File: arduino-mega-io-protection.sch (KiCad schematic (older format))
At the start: 29 parts, among them J101 CONN_01X02, J102 CONN_01X02, J103 CONN_01X02, J104 CONN_01X02, J105 CONN_01X02, J106 CONN_01X02, J107 CONN_01X02, J108 CONN_01X36, J109 CONN_01X10, J110 CONN_02X18, J111 CONN_01X08, J112 CONN_01X08, J113 CONN_01X08, J114 CONN_01X08, J115 CONN_01X08

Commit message: inserting part information for connectors into BOM
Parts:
- J109: MFN Value -> Sullins Connector Solutions; MPN Value -> PRPC010SAAN-RC; Populate (none) -> 1
- J112: MFN Value -> Sullins Connector Solutions; MPN Value -> PRPC008SAAN-RC; Populate (none) -> 1
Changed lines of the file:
@@
 F 2 "Pin_Headers:Pin_Header_Straight_1x10_Pitch2.54mm" H 9850 2250 50  0001 C CNN
 F 3 "" H 9850 2250 50  0001 C CNN
-F 4 "Value" H 9850 2250 60  0001 C CNN "MPN"
-F 5 "Value" H 9850 2250 60  0001 C CNN "MFN"
-F 6 "Value" H 9850 2250 60  0001 C CNN "Characteristics"
-F 7 "Value" H 9850 2250 60  0001 C CNN "Description"
-F 8 "Value" H 9850 2250 60  0001 C CNN "Package ID"
-F 9 "Digikey" H 9850 2250 60  0001 C CNN "Source"
-F 10 "Y" H 9850 2250 60  0001 C CNN "Critical"
-F 11 "X" H 9850 2250 60  0001 C CNN "Notes"
+F 4 "Value" H 9850 2250 60  0001 C CNN "Characteristics"
+F 5 "Value" H 9850 2250 60  0001 C CNN "Description"
+F 6 "Sullins Connector Solutions" H 9850 2250 60  0001 C CNN "MFN"
+F 7 "Value" H 9850 2250 60  0001 C CNN "Package ID"
+F 8 "Digikey" H 9850 2250 60  0001 C CNN "Source"
+F 9 "Y" H 9850 2250 60  0001 C CNN "Critical"
+F 10 "X" H 9850 2250 60  0001 C CNN "Notes"
+F 11 "1" H 9850 2250 60  0001 C CNN "Populate"
+F 12 "PRPC010SAAN-RC" H 9850 2250 60  0001 C CNN "MPN"
 	1    9850 2250
 	1    0    0    -1
@@
 F 2 "Pin_Headers:Pin_Header_Straight_1x08_Pitch2.54mm" H 9850 3250 50  0001 C CNN
 F 3 "" H 9850 3250 50  0001 C CNN
-F 4 "Value" H 9850 3250 60  0001 C CNN "MPN"
-F 5 "Value" H 9850 3250 60  0001 C CNN "MFN"
-F 6 "Value" H 9850 3250 60  0001 C CNN "Characteristics"
-F 7 "Value" H 9850 3250 60  0001 C CNN "Description"
-F 8 "Value" H 9850 3250 60  0001 C CNN "Package ID"
-F 9 "Digikey" H 9850 3250 60  0001 C CNN "Source"
-F 10 "Y" H 9850 3250 60  0001 C CNN "Critical"
-F 11 "X" H 9850 3250 60  0001 C CNN "Notes"
+F 4 "Value" H 9850 3250 60  0001 C CNN "Characteristics"
+F 5 "Value" H 9850 3250 60  0001 C CNN "Description"
+F 6 "Sullins Connector Solutions" H 9850 3250 60  0001 C CNN "MFN"
+F 7 "Value" H 9850 3250 60  0001 C CNN "Package ID"
+F 8 "Digikey" H 9850 3250 60  0001 C CNN "Source"
+F 9 "Y" H 9850 3250 60  0001 C CNN "Critical"
+F 10 "X" H 9850 3250 60  0001 C CNN "Notes"
+F 11 "1" H 9850 3250 60  0001 C CNN "Populate"
+F 12 "PRPC008SAAN-RC" H 9850 3250 60  0001 C CNN "MPN"
 	1    9850 3250
 	1    0    0    -1

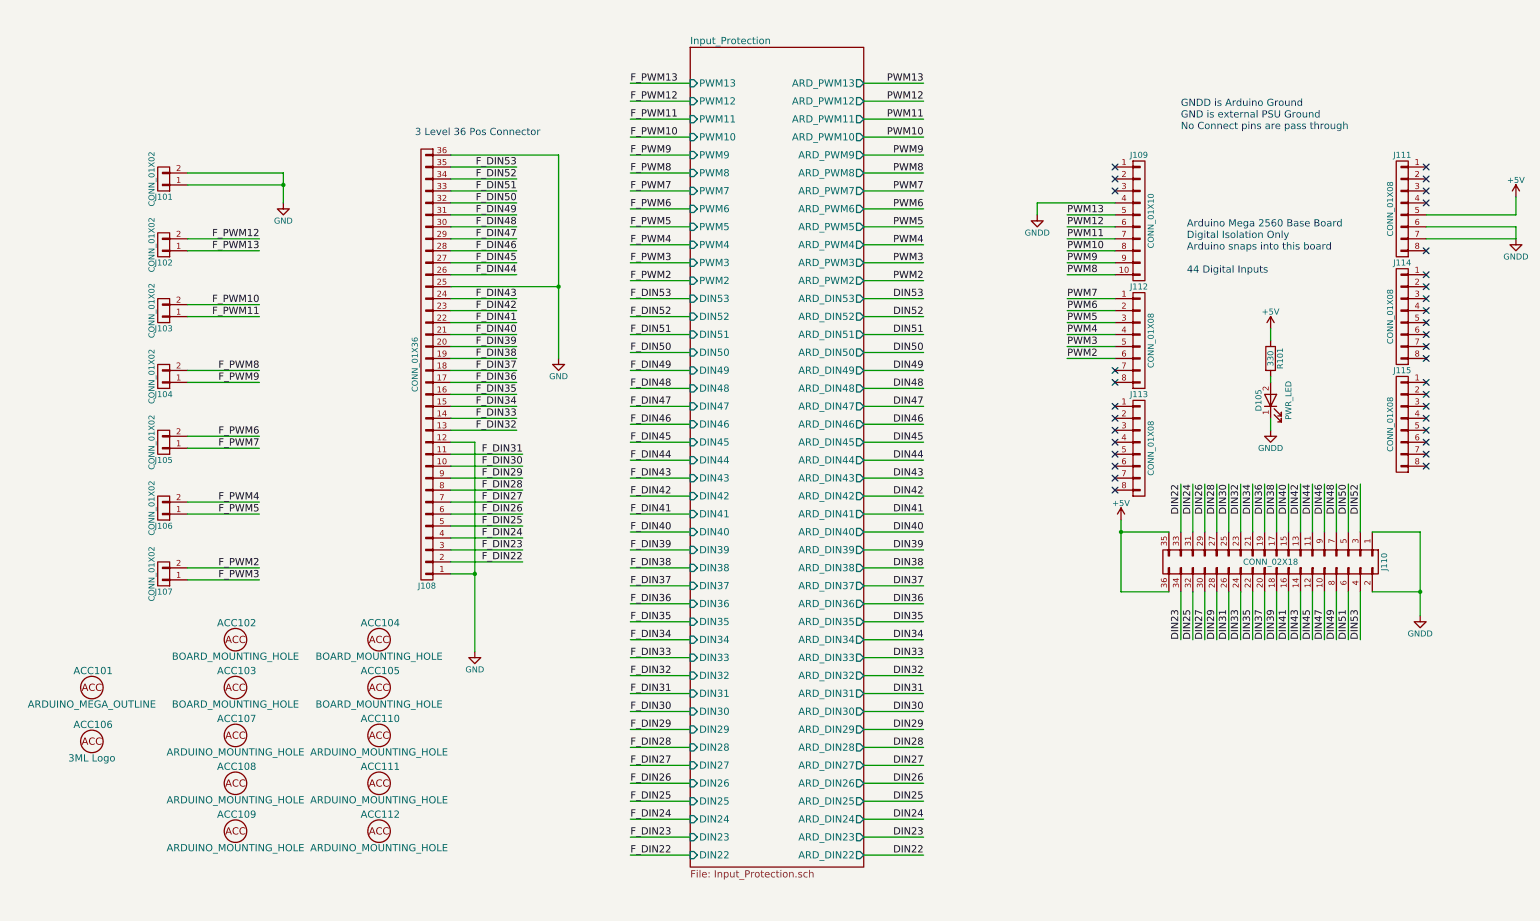
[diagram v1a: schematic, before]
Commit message: adding serial 1, 2, and 3 as protected inputs
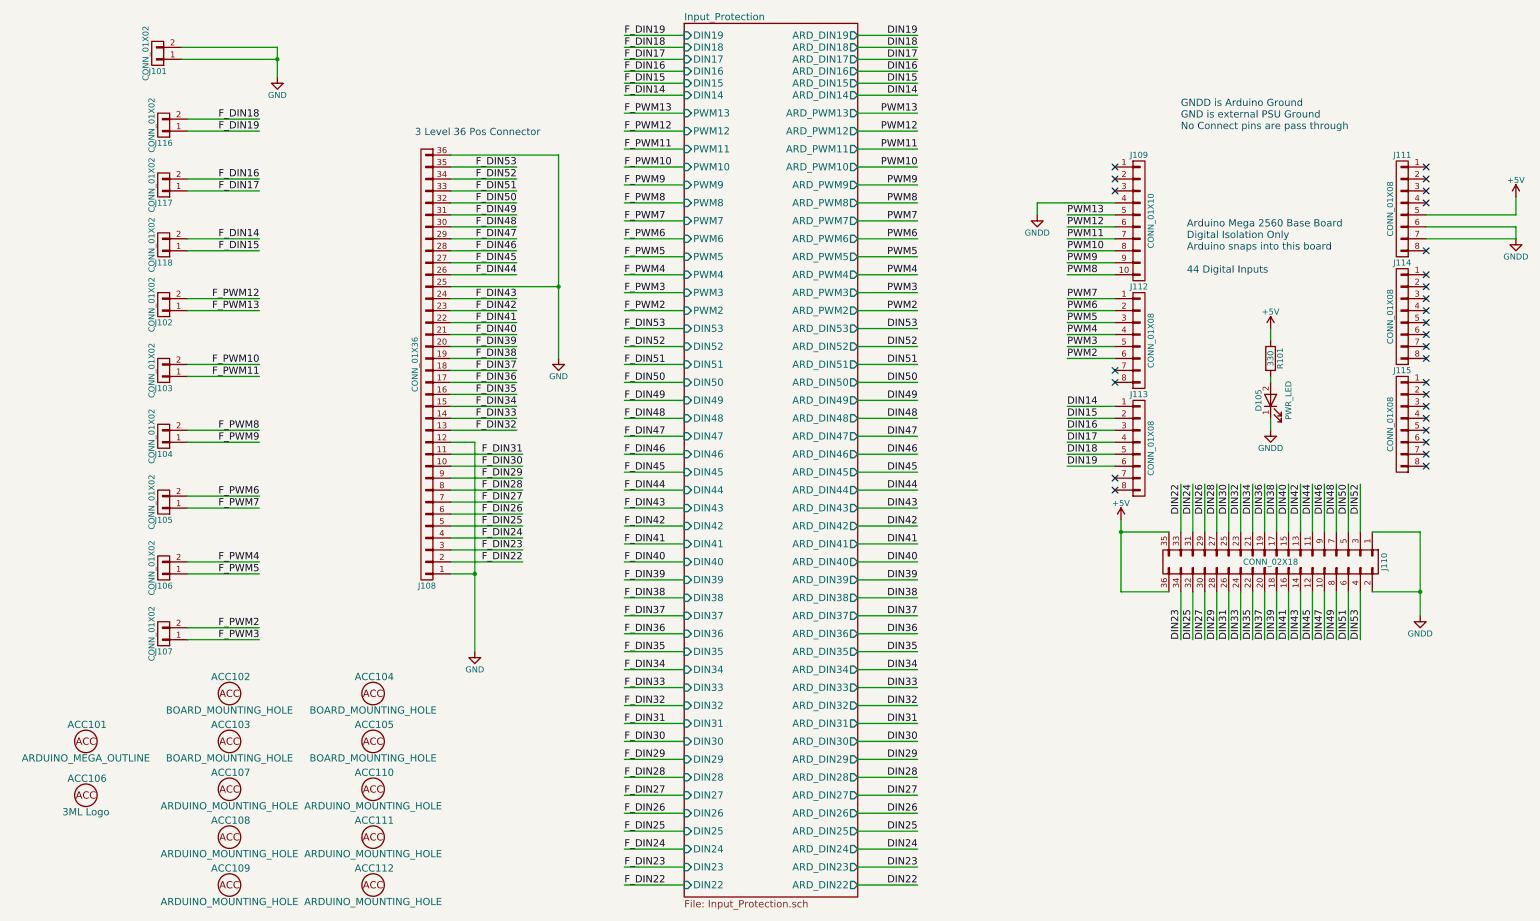
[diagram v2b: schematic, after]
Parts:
- added J116, J117, J118: CONN_01X02, 3ML_Footprint_Library:Wurth_691103010002, symbol CONN_01X02
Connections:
- net DIN14: now reaches J113.1 (P1)
- net DIN15: now reaches J113.2 (P2)
- net DIN16: now reaches J113.3 (P3)
- net DIN17: now reaches J113.4 (P4)
- net DIN18: now reaches J113.5 (P5)
- net DIN19: now reaches J113.6 (P6)
- new net F_DIN14: J118.2 (P2)
- new net F_DIN15: J118.1 (P1)
- new net F_DIN16: J117.2 (P2)
- new net F_DIN17: J117.1 (P1)
- new net F_DIN18: J116.2 (P2)
- new net F_DIN19: J116.1 (P1)
- no-connect marks 34 -> 28
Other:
- moved on the sheet: ACC101, ACC102, ACC103, ACC104, ACC105, ACC106, ACC107, ACC108, ACC109, ACC110, ACC111, ACC112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
